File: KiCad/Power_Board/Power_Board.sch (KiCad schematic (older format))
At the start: 21 parts, among them U1 AD1583, U2 MAX5259, U3 MAX5259

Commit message: Linked footprints to schematic.
Also cleaned up some footprint errors:
Changed IC footprint names to be invisible on the silkscreen layer.
Fixed test points that were lacking pin numbers causing netlist
failures.
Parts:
- C1: footprint (none) -> Capacitors_SMD:C_0805
- C2, C3, C4, C5, C6, C7: footprint (none) -> Capacitors_SMD:C_0603
- TP1, TP2, TP3, TP4, TP5, TP6, TP7, TP8: footprint (none) -> OpenCamera:TEST_CLIP
- TP28, TP29, TP9: footprint (none) -> OpenCamera:TEST_POINT_SMD
- U1: footprint (none) -> SMD_Packages:SOT-323
- U2, U3: footprint (none) -> OpenCamera:QSOP_16
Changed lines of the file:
@@
 F 0 "U1" H 4450 3800 60  0000 C CNN
 F 1 "AD1583" H 4450 3200 60  0000 C CNN
-F 2 "" H 4450 3500 60  0000 C CNN
+F 2 "SMD_Packages:SOT-323" H 4450 3500 60  0001 C CNN
 F 3 "" H 4450 3500 60  0000 C CNN
 	1    4450 3500
@@
 Vin
 $Comp
-L GND #PWR1
+L GND #PWR01
 U 1 1 5593D86A
 P 1600 4150
-F 0 "#PWR1" H 1600 3900 50  0001 C CNN
+F 0 "#PWR01" H 1600 3900 50  0001 C CNN
 F 1 "GND" H 1600 4000 50  0001 C CNN
 F 2 "" H 1600 4150 60  0000 C CNN
@@
 $EndComp
 $Comp
-L GND #PWR3
+L GND #PWR02
 U 1 1 5593E830
 P 2650 4150
-F 0 "#PWR3" H 2650 3900 50  0001 C CNN
+F 0 "#PWR02" H 2650 3900 50  0001 C CNN
 F 1 "GND" H 2650 4000 50  0001 C CNN
 F 2 "" H 2650 4150 60  0000 C CNN
@@
 Vin
 $Comp
-L GND #PWR5
+L GND #PWR03
 U 1 1 55940953
 P 3750 2800
-F 0 "#PWR5" H 3750 2550 50  0001 C CNN
+F 0 "#PWR03" H 3750 2550 50  0001 C CNN
 F 1 "GND" H 3750 2650 50  0001 C CNN
 F 2 "" H 3750 2800 60  0000 C CNN
@@
 $EndComp
 $Comp
-L GND #PWR4
+L GND #PWR04
 U 1 1 55940A3F
 P 3750 1500
-F 0 "#PWR4" H 3750 1250 50  0001 C CNN
+F 0 "#PWR04" H 3750 1250 50  0001 C CNN
 F 1 "GND" H 3750 1350 50  0001 C CNN
 F 2 "" H 3750 1500 60  0000 C CNN
@@
 Vref_3V
 $Comp
-L GND #PWR6
+L GND #PWR05
 U 1 1 559541BE
 P 3800 3700
-F 0 "#PWR6" H 3800 3450 50  0001 C CNN
+F 0 "#PWR05" H 3800 3450 50  0001 C CNN
 F 1 "GND" H 3800 3550 50  0001 C CNN
 F 2 "" H 3800 3700 60  0000 C CNN
@@
 F 0 "C2" H 3910 3570 50  0000 L CNN
 F 1 "0.1uF" H 3910 3420 50  0000 L CNN
-F 2 "" H 3900 3500 60  0000 C CNN
+F 2 "Capacitors_SMD:C_0603" H 3900 3500 60  0001 C CNN
 F 3 "" H 3900 3500 60  0000 C CNN
 	1    3900 3500
@@
 F 0 "C3" H 5010 3720 50  0000 L CNN
 F 1 "1uF" H 5010 3570 50  0000 L CNN
-F 2 "" H 5000 3650 60  0000 C CNN
+F 2 "Capacitors_SMD:C_0603" H 5000 3650 60  0001 C CNN
 F 3 "" H 5000 3650 60  0000 C CNN
 	1    5000 3650
@@
 F 0 "C1" H 3660 3570 50  0000 L CNN
 F 1 "4.7uF" H 3660 3420 50  0000 L CNN
-F 2 "" H 3650 3500 60  0000 C CNN
+F 2 "Capacitors_SMD:C_0805" H 3650 3500 60  0001 C CNN
 F 3 "" H 3650 3500 60  0000 C CNN
 	1    3650 3500
@@
 $EndComp
 $Comp
-L GND #PWR7
+L GND #PWR06
 U 1 1 5596E916
 P 5000 3800
-F 0 "#PWR7" H 5000 3550 50  0001 C CNN
+F 0 "#PWR06" H 5000 3550 50  0001 C CNN
 F 1 "GND" H 5000 3650 50  0001 C CNN
 F 2 "" H 5000 3800 60  0000 C CNN
@@
 F 0 "TP2" H 2300 7600 60  0000 C CNN
 F 1 "Test_Point" H 2300 7700 60  0001 C CNN
-F 2 "" H 2300 7350 60  0000 C CNN
+F 2 "OpenCamera:TEST_CLIP" H 2300 7350 60  0001 C CNN
 F 3 "" H 2300 7350 60  0000 C CNN
 	1    2300 7350
@@
 F 0 "TP3" H 2650 7600 60  0000 C CNN
 F 1 "Test_Point" H 2650 7700 60  0001 C CNN
-F 2 "" H 2650 7350 60  0000 C CNN
+F 2 "OpenCamera:TEST_CLIP" H 2650 7350 60  0001 C CNN
 F 3 "" H 2650 7350 60  0000 C CNN
 	1    2650 7350
@@
 F 0 "TP4" H 3000 7600 60  0000 C CNN
 F 1 "Test_Point" H 3000 7700 60  0001 C CNN
-F 2 "" H 3000 7350 60  0000 C CNN
+F 2 "OpenCamera:TEST_CLIP" H 3000 7350 60  0001 C CNN
 F 3 "" H 3000 7350 60  0000 C CNN
 	1    3000 7350
@@
 F 0 "TP5" H 3350 7600 60  0000 C CNN
 F 1 "Test_Point" H 3350 7700 60  0001 C CNN
-F 2 "" H 3350 7350 60  0000 C CNN
+F 2 "OpenCamera:TEST_CLIP" H 3350 7350 60  0001 C CNN
 F 3 "" H 3350 7350 60  0000 C CNN
 	1    3350 7350
@@
 F 0 "TP7" H 4050 7600 60  0000 C CNN
 F 1 "Test_Point" H 4050 7700 60  0001 C CNN
-F 2 "" H 4050 7350 60  0000 C CNN
+F 2 "OpenCamera:TEST_CLIP" H 4050 7350 60  0001 C CNN
 F 3 "" H 4050 7350 60  0000 C CNN
 	1    4050 7350
@@
 F 0 "TP6" H 3700 7600 60  0000 C CNN
 F 1 "Test_Point" H 3700 7700 60  0001 C CNN
-F 2 "" H 3700 7350 60  0000 C CNN
+F 2 "OpenCamera:TEST_CLIP" H 3700 7350 60  0001 C CNN
 F 3 "" H 3700 7350 60  0000 C CNN
 	1    3700 7350
@@
 F 0 "TP9" H 5200 3700 60  0000 C CNN
 F 1 "Test_Point" H 5200 3800 60  0001 C CNN
-F 2 "" H 5200 3450 60  0000 C CNN
+F 2 "OpenCamera:TEST_POINT_SMD" H 5200 3450 60  0001 C CNN
 F 3 "" H 5200 3450 60  0000 C CNN
 	1    5200 3450
@@
 F 0 "TP8" H 4400 7600 60  0000 C CNN
 F 1 "Test_Point" H 4400 7700 60  0001 C CNN
-F 2 "" H 4400 7350 60  0000 C CNN
+F 2 "OpenCamera:TEST_CLIP" H 4400 7350 60  0001 C CNN
 F 3 "" H 4400 7350 60  0000 C CNN
 	1    4400 7350
@@
 $EndComp
 $Comp
-L GND #PWR2
+L GND #PWR07
 U 1 1 55930F58
 P 1950 7400
-F 0 "#PWR2" H 1950 7150 50  0001 C CNN
+F 0 "#PWR07" H 1950 7150 50  0001 C CNN
 F 1 "GND" H 1950 7250 50  0001 C CNN
 F 2 "" H 1950 7400 60  0000 C CNN
@@
 F 0 "TP1" H 1950 7600 60  0000 C CNN
 F 1 "Test_Point" H 1950 7700 60  0001 C CNN
-F 2 "" H 1950 7350 60  0000 C CNN
+F 2 "OpenCamera:TEST_CLIP" H 1950 7350 60  0001 C CNN
 F 3 "" H 1950 7350 60  0000 C CNN
 	1    1950 7350
@@
 F 0 "U2" H 8450 2750 60  0000 C CNN
 F 1 "MAX5259" H 8450 1750 60  0000 C CNN
-F 2 "" H 8450 2250 60  0000 C CNN
+F 2 "OpenCamera:QSOP_16" H 8450 2250 60  0001 C CNN
 F 3 "" H 8450 2250 60  0000 C CNN
 	1    8450 2250
@@
 MOSI
 $Comp
-L GND #PWR10
+L GND #PWR08
 U 1 1 55976AA8
 P 7750 2650
-F 0 "#PWR10" H 7750 2400 50  0001 C CNN
+F 0 "#PWR08" H 7750 2400 50  0001 C CNN
 F 1 "GND" H 7750 2500 50  0001 C CNN
 F 2 "" H 7750 2650 60  0000 C CNN
@@
 F 0 "TP28" H 7100 2550 60  0000 C CNN
 F 1 "Test_Point" H 7100 2650 60  0001 C CNN
-F 2 "" H 7100 2300 60  0000 C CNN
+F 2 "OpenCamera:TEST_POINT_SMD" H 7100 2300 60  0001 C CNN
 F 3 "" H 7100 2300 60  0000 C CNN
 	1    7100 2300
@@
 F 0 "C4" H 7350 1800 50  0000 L CNN
 F 1 "1uF" H 7350 1650 50  0000 L CNN
-F 2 "" H 7350 1750 60  0000 C CNN
+F 2 "Capacitors_SMD:C_0603" H 7350 1750 60  0001 C CNN
 F 3 "" H 7350 1750 60  0000 C CNN
 	1    7350 1750
@@
 F 0 "C6" H 7550 1800 50  0000 L CNN
 F 1 "0.1uF" H 7550 1650 50  0000 L CNN
-F 2 "" H 7550 1750 60  0000 C CNN
+F 2 "Capacitors_SMD:C_0603" H 7550 1750 60  0001 C CNN
 F 3 "" H 7550 1750 60  0000 C CNN
 	1    7550 1750
@@
 $EndComp
 $Comp
-L GND #PWR8
+L GND #PWR09
 U 1 1 5598353D
 P 7100 1550
-F 0 "#PWR8" H 7100 1300 50  0001 C CNN
+F 0 "#PWR09" H 7100 1300 50  0001 C CNN
 F 1 "GND" H 7100 1400 50  0001 C CNN
 F 2 "" H 7100 1550 60  0000 C CNN
@@
 F 0 "U3" H 8500 4700 60  0000 C CNN
 F 1 "MAX5259" H 8500 3700 60  0000 C CNN
-F 2 "" H 8500 4200 60  0000 C CNN
+F 2 "OpenCamera:QSOP_16" H 8500 4200 60  0001 C CNN
 F 3 "" H 8500 4200 60  0000 C CNN
 	1    8500 4200
@@
 MOSI
 $Comp
-L GND #PWR11
+L GND #PWR010
 U 1 1 559888C5
 P 7800 4600
-F 0 "#PWR11" H 7800 4350 50  0001 C CNN
+F 0 "#PWR010" H 7800 4350 50  0001 C CNN
 F 1 "GND" H 7800 4450 50  0001 C CNN
 F 2 "" H 7800 4600 60  0000 C CNN
@@
 F 0 "TP29" H 7100 4500 60  0000 C CNN
 F 1 "Test_Point" H 7100 4600 60  0001 C CNN
-F 2 "" H 7100 4250 60  0000 C CNN
+F 2 "OpenCamera:TEST_POINT_SMD" H 7100 4250 60  0001 C CNN
 F 3 "" H 7100 4250 60  0000 C CNN
 	1    7100 4250
@@
 F 0 "C5" H 7400 3750 50  0000 L CNN
 F 1 "1uF" H 7400 3600 50  0000 L CNN
-F 2 "" H 7400 3700 60  0000 C CNN
+F 2 "Capacitors_SMD:C_0603" H 7400 3700 60  0001 C CNN
 F 3 "" H 7400 3700 60  0000 C CNN
 	1    7400 3700
@@
 F 0 "C7" H 7600 3750 50  0000 L CNN
 F 1 "0.1uF" H 7600 3600 50  0000 L CNN
-F 2 "" H 7600 3700 60  0000 C CNN
+F 2 "Capacitors_SMD:C_0603" H 7600 3700 60  0001 C CNN
 F 3 "" H 7600 3700 60  0000 C CNN
 	1    7600 3700
@@
 $EndComp
 $Comp
-L GND #PWR9
+L GND #PWR011
 U 1 1 559888EE
 P 7150 3500
-F 0 "#PWR9" H 7150 3250 50  0001 C CNN
+F 0 "#PWR011" H 7150 3250 50  0001 C CNN
 F 1 "GND" H 7150 3350 50  0001 C CNN
 F 2 "" H 7150 3500 60  0000 C CNN

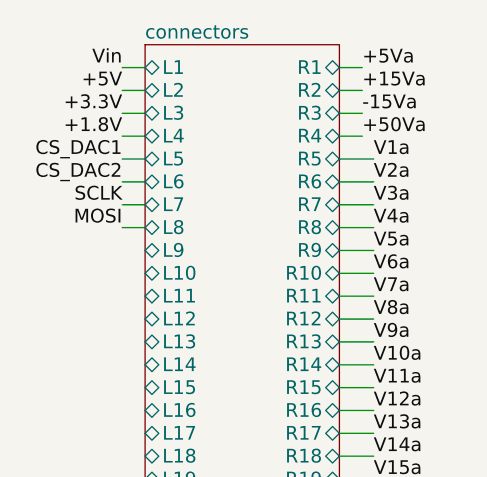
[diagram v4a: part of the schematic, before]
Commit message: Added a reserved MISO pin on the board-board connectors for future SPI devices.
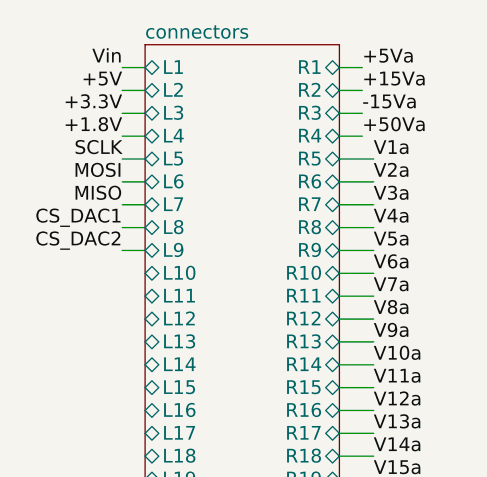
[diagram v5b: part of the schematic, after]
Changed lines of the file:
@@
 	7400 3600 7400 3400
 Connection ~ 7400 3400
+Text Label 1600 1600 2    60   ~ 0
+CS_DAC1
 Text Label 1600 1300 2    60   ~ 0
-CS_DAC1
+SCLK
+Text Label 1600 1400 2    60   ~ 0
+MOSI
+Text Label 1600 1700 2    60   ~ 0
+CS_DAC2
 Text Label 1600 1500 2    60   ~ 0
-SCLK
-Text Label 1600 1600 2    60   ~ 0
-MOSI
-Text Label 1600 1400 2    60   ~ 0
-CS_DAC2
+MISO
 Wire Wire Line
-	1700 1300 1600 1300
+	1600 1300 1700 1300
 Wire Wire Line
-	1700 1400 1600 1400
+	1600 1400 1700 1400
 Wire Wire Line
-	1700 1500 1600 1500
+	1600 1500 1700 1500
 Wire Wire Line
-	1700 1600 1600 1600
+	1600 1600 1700 1600
+Wire Wire Line
+	1600 1700 1700 1700
 $EndSCHEMATC

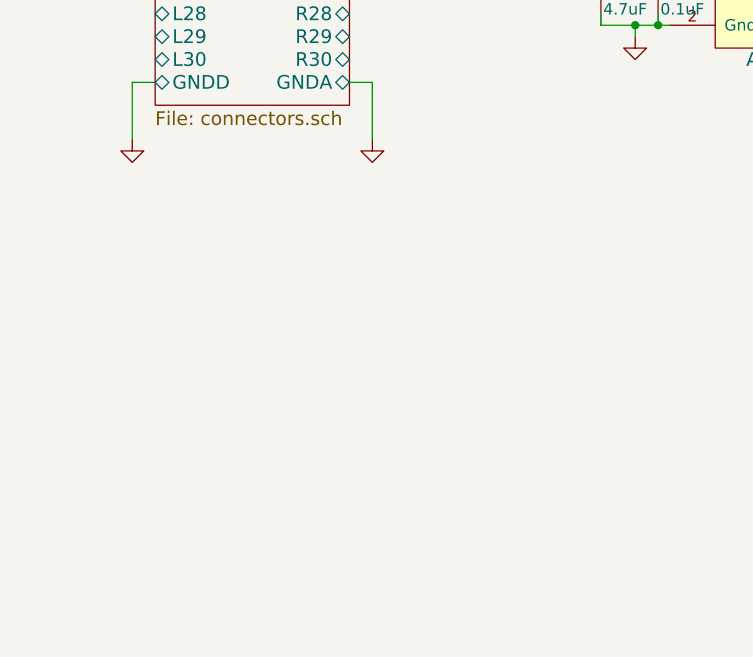
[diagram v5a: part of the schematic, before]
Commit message: Connected GND & GNDA since this is the power board which supplies both.
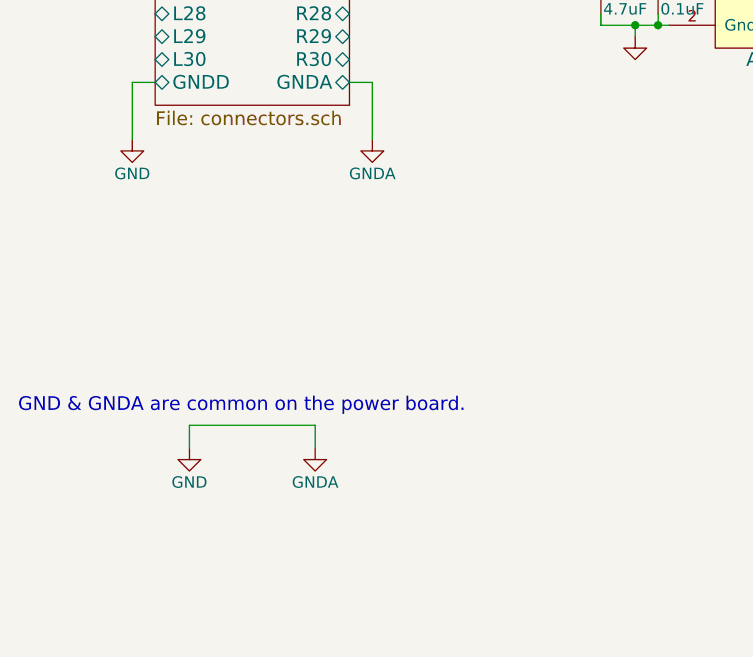
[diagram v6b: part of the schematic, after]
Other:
- note added: "GND & GNDA are common on the power board."
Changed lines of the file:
@@
 P 1600 4150
 F 0 "#PWR01" H 1600 3900 50  0001 C CNN
-F 1 "GND" H 1600 4000 50  0001 C CNN
+F 1 "GND" H 1600 4000 50  0000 C CNN
 F 2 "" H 1600 4150 60  0000 C CNN
 F 3 "" H 1600 4150 60  0000 C CNN
 	1    1600 4150
-	1    0    0    -1
-$EndComp
-$Comp
-L GND #PWR02
-U 1 1 5593E830
-P 2650 4150
-F 0 "#PWR02" H 2650 3900 50  0001 C CNN
-F 1 "GND" H 2650 4000 50  0001 C CNN
-F 2 "" H 2650 4150 60  0000 C CNN
-F 3 "" H 2650 4150 60  0000 C CNN
-	1    2650 4150
 	1    0    0    -1
 $EndComp
@@
 Wire Wire Line
 	1600 1700 1700 1700
+$Comp
+L GNDA #PWR?
+U 1 1 5599A693
+P 2650 4150
+F 0 "#PWR?" H 2650 3900 50  0001 C CNN
+F 1 "GNDA" H 2650 4000 50  0000 C CNN
+F 2 "" H 2650 4150 60  0000 C CNN
+F 3 "" H 2650 4150 60  0000 C CNN
+	1    2650 4150
+	1    0    0    -1
+$EndComp
+$Comp
+L GNDA #PWR?
+U 1 1 5599CD2A
+P 2400 5500
+F 0 "#PWR?" H 2400 5250 50  0001 C CNN
+F 1 "GNDA" H 2400 5350 50  0000 C CNN
+F 2 "" H 2400 5500 60  0000 C CNN
+F 3 "" H 2400 5500 60  0000 C CNN
+	1    2400 5500
+	1    0    0    -1
+$EndComp
+$Comp
+L GND #PWR?
+U 1 1 5599D6AA
+P 1850 5500
+F 0 "#PWR?" H 1850 5250 50  0001 C CNN
+F 1 "GND" H 1850 5350 50  0000 C CNN
+F 2 "" H 1850 5500 60  0000 C CNN
+F 3 "" H 1850 5500 60  0000 C CNN
+	1    1850 5500
+	1    0    0    -1
+$EndComp
+Wire Wire Line
+	1850 5500 1850 5400
+Wire Wire Line
+	1850 5400 2400 5400
+Wire Wire Line
+	2400 5400 2400 5500
+Text Notes 1100 5350 0    60   ~ 0
+GND & GNDA are common on the power board.
 $EndSCHEMATC

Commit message: Some layout progress.
Properly placed and oriented parts for compact layout of individual
modules.
Added zones of copper around the converters as appropriate.
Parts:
- removed TP28, TP29: Test_Point, OpenCamera:TEST_POINT_SMD, symbol Test_Point
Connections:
- net V10a: now also U3.10 (OUTH); no longer U3.1 (OUTB)
- net V11a: now also U3.15 (OUTD); no longer U3.16 (OUTC)
- net V12a: now also U3.16 (OUTC); no longer U3.15 (OUTD)
- net V13a: now also U3.1 (OUTB); no longer U3.7 (OUTE)
- net V14a: now also U3.2 (OUTA); no longer U3.8 (OUTF)
- net V15a: now also U3.7 (OUTE); no longer U3.9 (OUTG)
- net V16a: now also U3.8 (OUTF); no longer U3.10 (OUTH)
- net V1a: now also U2.1 (OUTB); no longer U2.2 (OUTA)
- net V2a: now also U2.2 (OUTA); no longer U2.1 (OUTB)
- net V3a: now also U2.7 (OUTE); no longer U2.16 (OUTC)
- net V4a: now also U2.8 (OUTF); no longer U2.15 (OUTD)
- net V5a: now also U2.9 (OUTG); no longer U2.7 (OUTE)
- net V6a: now also U2.10 (OUTH); no longer U2.8 (OUTF)
- net V7a: now also U2.15 (OUTD); no longer U2.9 (OUTG)
- net V8a: now also U2.16 (OUTC); no longer U2.10 (OUTH)
- net V9a: now also U3.9 (OUTG); no longer U3.2 (OUTA)
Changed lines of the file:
@@
 Sheet 1 4
 Title "Power Board"
-Date "Friday, July 03, 2015"
+Date "Sunday, July 05, 2015"
 Rev "1.1"
 Comp "Open Camera Project"
@@
 Text Label 2700 2800 0    60   ~ 0
 V16a
+Text Label 9200 2000 0    60   ~ 0
+V1a
 Text Label 9200 1900 0    60   ~ 0
-V1a
-Text Label 9200 2000 0    60   ~ 0
 V2a
+Text Label 9200 2300 0    60   ~ 0
+V3a
+Text Label 9200 2400 0    60   ~ 0
+V4a
+Text Label 9200 2500 0    60   ~ 0
+V5a
+Text Label 9200 2600 0    60   ~ 0
+V6a
+Text Label 9200 2200 0    60   ~ 0
+V7a
 Text Label 9200 2100 0    60   ~ 0
-V3a
-Text Label 9200 2200 0    60   ~ 0
-V4a
-Text Label 9200 2300 0    60   ~ 0
-V5a
-Text Label 9200 2400 0    60   ~ 0
-V6a
-Text Label 9200 2500 0    60   ~ 0
-V7a
-Text Label 9200 2600 0    60   ~ 0
 V8a
 Text Notes 3050 6950 0    60   ~ 0
@@
 Wire Wire Line
 	7800 2100 7700 2100
-$Comp
-L Test_Point TP28
-U 1 1 55978320
-P 7100 2300
-F 0 "TP28" H 7100 2550 60  0000 C CNN
-F 1 "Test_Point" H 7100 2650 60  0001 C CNN
-F 2 "OpenCamera:TEST_POINT_SMD" H 7100 2300 60  0001 C CNN
-F 3 "" H 7100 2300 60  0000 C CNN
-	1    7100 2300
-	1    0    0    -1
-$EndComp
-Wire Wire Line
-	7800 2400 7100 2400
-Wire Wire Line
-	7100 2400 7100 2300
 Wire Wire Line
 	7800 2500 7750 2500
 Connection ~ 7750 2600
-Wire Wire Line
-	9200 1900 9100 1900
-Wire Wire Line
-	9200 2000 9100 2000
-Wire Wire Line
-	9200 2100 9100 2100
-Wire Wire Line
-	9200 2200 9100 2200
-Wire Wire Line
-	9200 2300 9100 2300
-Wire Wire Line
-	9200 2400 9100 2400
-Wire Wire Line
-	9200 2500 9100 2500
-Wire Wire Line
-	9200 2600 9100 2600
 $Comp
 L C_Small C4
@@
 	7350 1650 7350 1450
 Connection ~ 7350 1450
+Text Label 9250 4450 0    60   ~ 0
+V9a
+Text Label 9250 4550 0    60   ~ 0
+V10a
+Text Label 9250 4150 0    60   ~ 0
+V11a
+Text Label 9250 4050 0    60   ~ 0
+V12a
+Text Label 9250 3950 0    60   ~ 0
+V13a
 Text Label 9250 3850 0    60   ~ 0
-V9a
-Text Label 9250 3950 0    60   ~ 0
-V10a
-Text Label 9250 4050 0    60   ~ 0
-V11a
-Text Label 9250 4150 0    60   ~ 0
-V12a
+V14a
 Text Label 9250 4250 0    60   ~ 0
-V13a
+V15a
 Text Label 9250 4350 0    60   ~ 0
-V14a
-Text Label 9250 4450 0    60   ~ 0
-V15a
-Text Label 9250 4550 0    60   ~ 0
 V16a
 $Comp
@@
 Wire Wire Line
 	7850 4050 7750 4050
-$Comp
-L Test_Point TP29
-U 1 1 559888D0
-P 7100 4250
-F 0 "TP29" H 7100 4500 60  0000 C CNN
-F 1 "Test_Point" H 7100 4600 60  0001 C CNN
-F 2 "OpenCamera:TEST_POINT_SMD" H 7100 4250 60  0001 C CNN
-F 3 "" H 7100 4250 60  0000 C CNN
-	1    7100 4250
-	1    0    0    -1
-$EndComp
-Wire Wire Line
-	7850 4350 7100 4350
-Wire Wire Line
-	7100 4350 7100 4250
 Wire Wire Line
 	7850 4450 7800 4450
 Connection ~ 7800 4550
-Wire Wire Line
-	9250 3850 9150 3850
-Wire Wire Line
-	9250 3950 9150 3950
-Wire Wire Line
-	9250 4050 9150 4050
-Wire Wire Line
-	9250 4150 9150 4150
-Wire Wire Line
-	9250 4250 9150 4250
-Wire Wire Line
-	9250 4350 9150 4350
-Wire Wire Line
-	9250 4450 9150 4450
-Wire Wire Line
-	9250 4550 9150 4550
 $Comp
 L C_Small C5
@@
 Text Notes 1100 5350 0    60   ~ 0
 GND & GNDA are common on the power board.
+Wire Wire Line
+	9100 1900 9200 1900
+Wire Wire Line
+	9100 2000 9200 2000
+Wire Wire Line
+	9100 2100 9200 2100
+Wire Wire Line
+	9100 2200 9200 2200
+Wire Wire Line
+	9100 2300 9200 2300
+Wire Wire Line
+	9100 2400 9200 2400
+Wire Wire Line
+	9100 2500 9200 2500
+Wire Wire Line
+	9100 2600 9200 2600
+Wire Wire Line
+	9150 3850 9250 3850
+Wire Wire Line
+	9150 3950 9250 3950
+Wire Wire Line
+	9150 4050 9250 4050
+Wire Wire Line
+	9150 4150 9250 4150
+Wire Wire Line
+	9150 4250 9250 4250
+Wire Wire Line
+	9150 4350 9250 4350
+Wire Wire Line
+	9150 4450 9250 4450
+Wire Wire Line
+	9150 4550 9250 4550
 $EndSCHEMATC
